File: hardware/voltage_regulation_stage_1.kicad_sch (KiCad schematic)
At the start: 21 parts, among them IC3 LT8333RDD#TRPBF

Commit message: Continued work on schematic.
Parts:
- added Q2: PMOS, symbol Simulation_SPICE:PMOS
- added Q5: MUN5314DW1T1G, Package_TO_SOT_SMD:SOT-363_SC-70-6, symbol Device:Q_Dual_NPN_PNP_BRT_E1B1C2E2B2C1
- added Q7: NMOS, symbol Simulation_SPICE:NMOS
- added R52, R53: R_Small_US, symbol Device:R_Small_US
- added R56, R57: ~, symbol Device:R_Small_US
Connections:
- net GND: now also Q7.1 (D), Q7.3 (S), R53.2, R57.2
- net VREG1_POWER: now reaches C34.1, L3.1
- net at C36.1, L4.2: now also Q2.3 (S), Q5.4 (E1), R56.1
- new net: Q2.2 (G), R56.2, R57.1
- new net: Q5.1 (E1), Q5.3 (C1), R52.1
- new net: Q5.5 (B1), Q5.6 (C1)
- new net: R52.2, R53.1
- new net VREG2_POWER: Q2.1 (D)
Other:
- moved on the sheet: C25, C26, C27, C28, C29, C30, C31, C32, C33, C34, C35, C36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

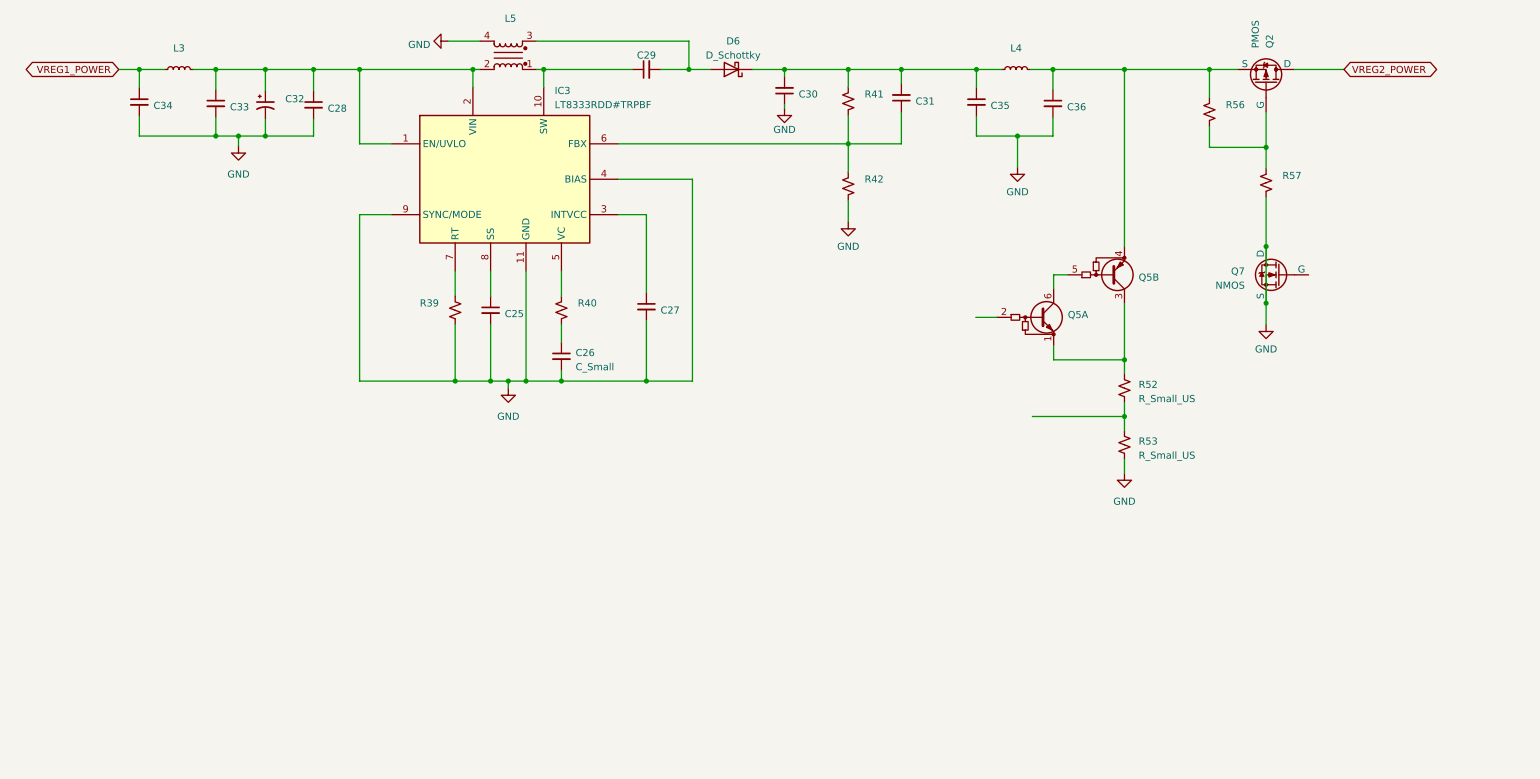
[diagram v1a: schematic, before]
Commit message: Component values chosen for bat. charge, bat. protect, USB input
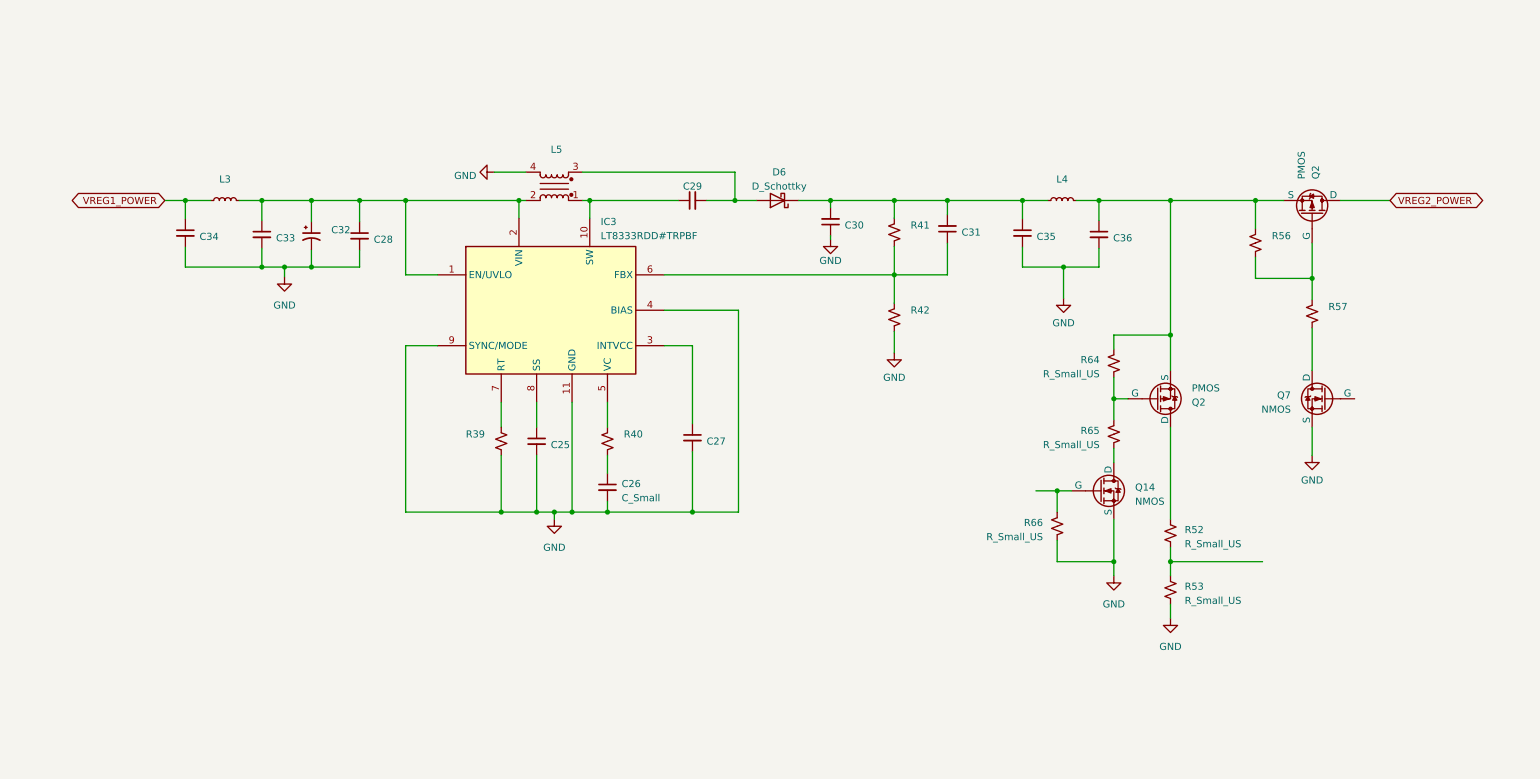
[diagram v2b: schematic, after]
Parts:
- removed Q5: MUN5314DW1T1G, Package_TO_SOT_SMD:SOT-363_SC-70-6, symbol Device:Q_Dual_NPN_PNP_BRT_E1B1C2E2B2C1
- added Q14: NMOS, symbol Simulation_SPICE:NMOS
- added Q2: PMOS, symbol Simulation_SPICE:PMOS
- added R64, R65, R66: R_Small_US, symbol Device:R_Small_US
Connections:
- net GND: now also Q14.3 (S), R66.2; no longer Q7.1 (D), R57.2
- net at C36.1, L4.2, Q2.3 (S)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: now also Q2.3 (S), R64.1
- net at R52.1: now also Q2.1 (D)
- new net: Q14.1 (D), R65.2
- new net: Q14.2 (G), R66.1
- new net: Q7.1 (D), R57.2
- new net: Q2.2 (G), R64.2, R65.1
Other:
- moved on the sheet: C25, C26, C27, C28, C29, C30, C31, C32, C33, C34, C35, C36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

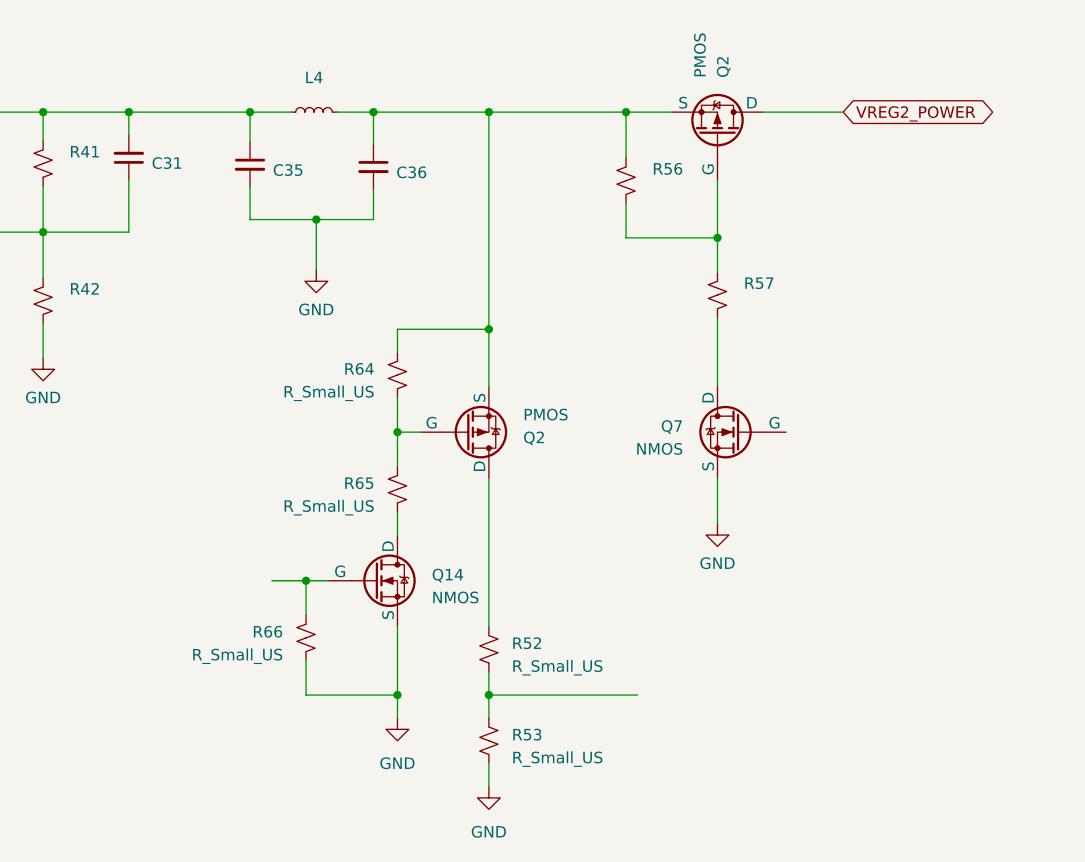
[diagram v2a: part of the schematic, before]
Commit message: Most work finished on stage1. Moving on to stage2.
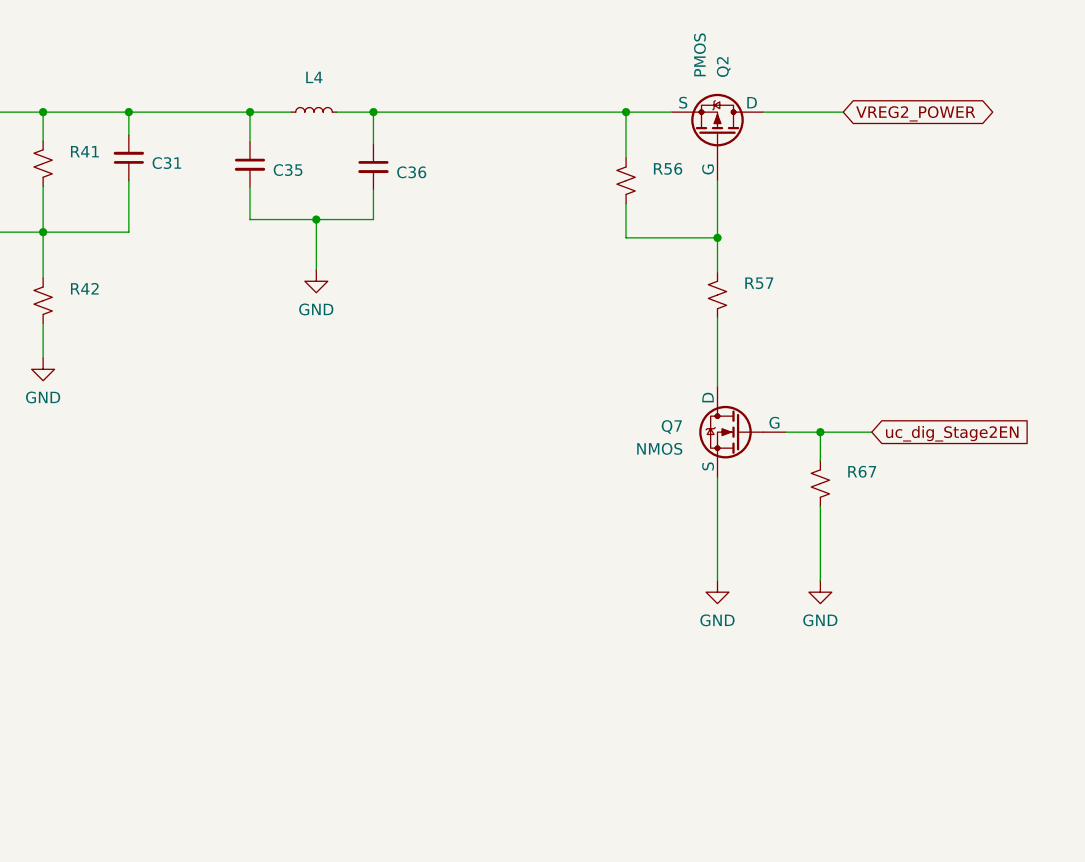
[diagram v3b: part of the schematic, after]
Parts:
- removed Q14: NMOS, symbol Simulation_SPICE:NMOS
- removed Q2: PMOS, symbol Simulation_SPICE:PMOS
- removed R52, R53, R64, R65, R66: R_Small_US, symbol Device:R_Small_US
- added R67: ~, symbol Device:R_Small_US
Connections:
- net GND: now also R67.2
- net uc_dig_Stage2EN: now reaches Q7.2 (G)
- net uc_dig_Stage2EN: now also R67.1

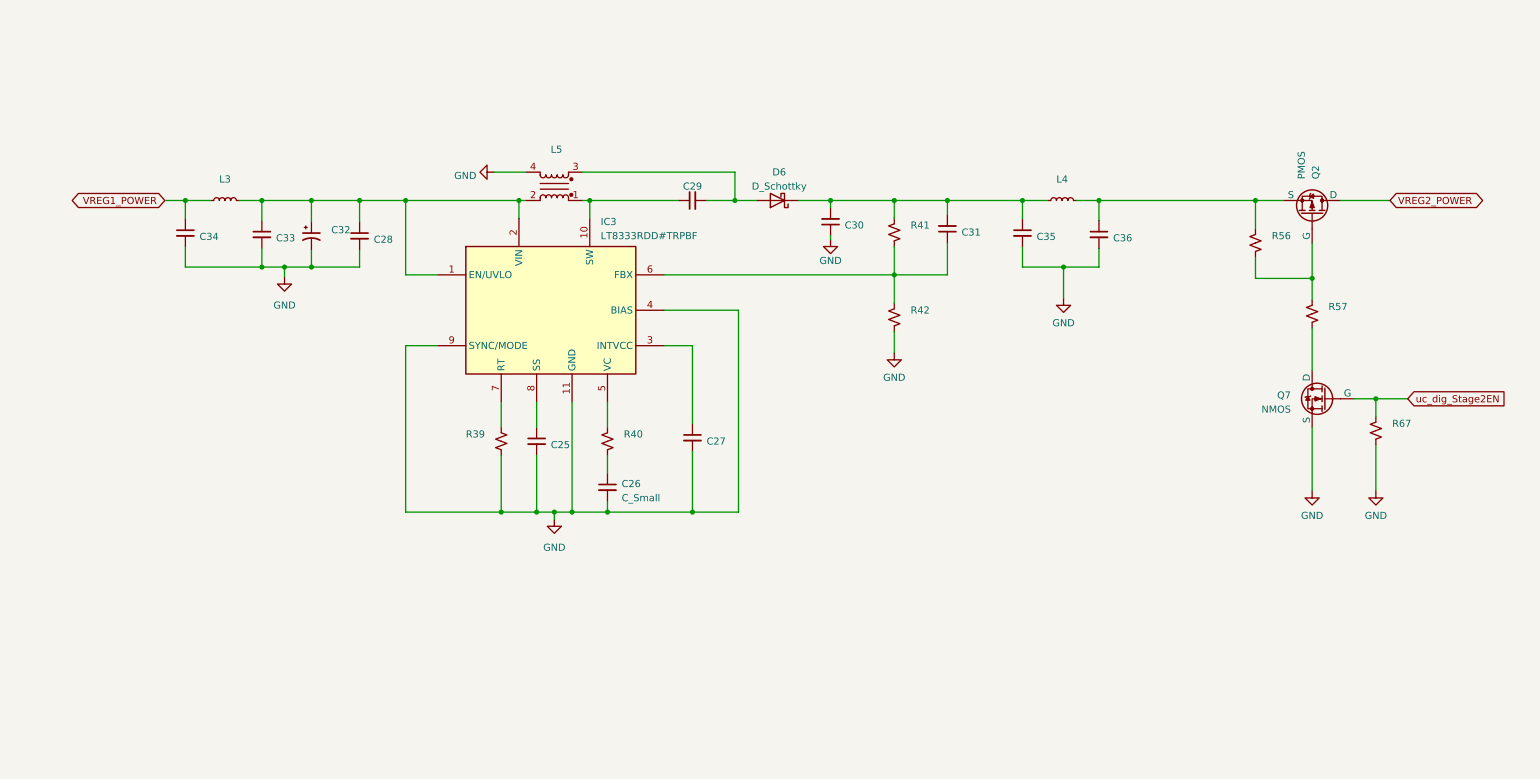
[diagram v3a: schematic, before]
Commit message: More simulation and work done on SEPIC stage. MOSFET changes to USB stage and charging stage.
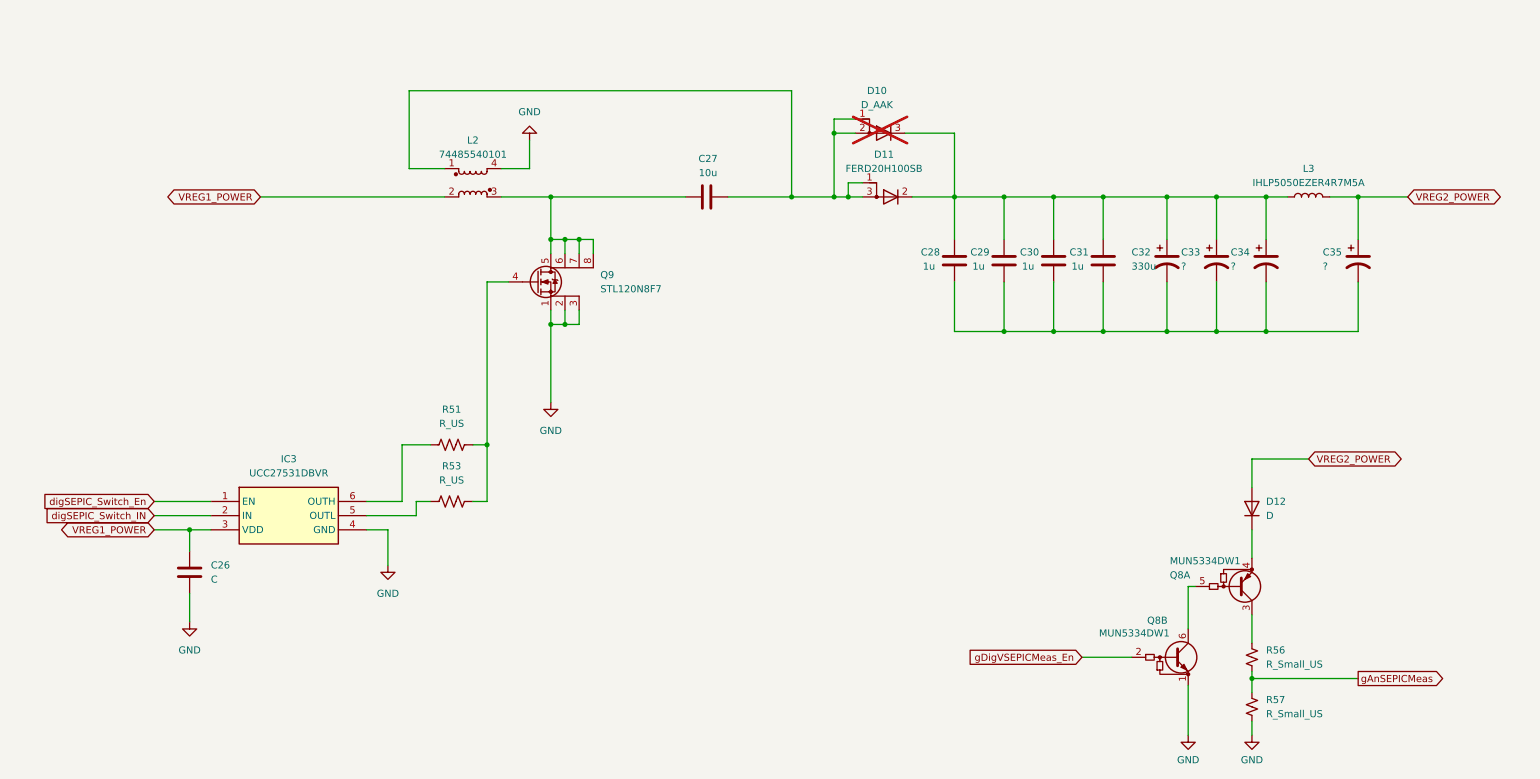
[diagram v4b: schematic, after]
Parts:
- removed C25, C27, C28, C29, C30, C31, C33, C34, C35, C36: ~, symbol Device:C_Small
- removed C26: C_Small, symbol Device:C_Small
- removed C32: C_Polarized_Small_US, symbol Device:C_Polarized_Small_US
- removed D6: D_Schottky, symbol Device:D_Schottky
- removed IC3: LT8333RDD#TRPBF, SON50P300X300X80-11N-D, symbol LT8333RDD#TRPBF:LT8333RDD#TRPBF
- removed L3, L4: L_Small, symbol Device:L_Small
- removed L5: L_Iron_Coupled, symbol Device:L_Iron_Coupled
- removed Q2: PMOS, symbol Simulation_SPICE:PMOS
- removed Q7: NMOS, symbol Simulation_SPICE:NMOS
- removed R39, R40, R41, R42, R67: ~, symbol Device:R_Small_US
- added C26: C, symbol Device:C
- added C27: 10u, symbol Device:C
- added C28, C29, C30, C31: 1u, symbol Device:C
- added C32: 330u, symbol Device:C_Polarized_US
- added C33, C34, C35: ?, symbol Device:C_Polarized_US
- added D10: D_AAK, Package_TO_SOT_SMD:TO-277A, symbol Device:D_AAK
- added D11: FERD20H100SB, symbol Daniel_Diode:D_AKA
- added D12: D, symbol Device:D
- added IC3: UCC27531DBVR, Package_TO_SOT_SMD:SOT-23-6, symbol Daniel_Gate-Driver:UCC27531DBVR
- added L2: 74485540101, Daniel_Inductor:74485540101, symbol Daniel_Inductor:L_Coupled
- added L3: IHLP5050EZER4R7M5A, Daniel_Inductor:IHLP-5050EZ, symbol Device:L
- added Q8: MUN5334DW1, Package_TO_SOT_SMD:SOT-363_SC-70-6, symbol Transistor_BJT:MUN5334DW1
- added Q9: STL120N8F7, Package_SON:ST_PowerFLAT-6L_5x6mm_P1.27mm, symbol Daniel_NMOS:Q_NMOS_DGS
- added R51, R53: R_US, symbol Device:R_US
- R56, R57: value ~ -> R_Small_US
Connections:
- net GND: now also R57.1, C26.2, IC3.4 (GND), L2.4, Q8.1 (E2), Q9.1 (S), Q9.2 (S), Q9.3 (S)
- net VREG1_POWER: now also C26.1, IC3.3 (VDD), L2.2
- net VREG2_POWER: now also C35.1, D12.2 (A), L3.2
- net gAnSEPICMeas: now reaches R56.1
- net gAnSEPICMeas: now also R57.2
- net at R56.2: now also Q8.3 (C1); no longer R57.1
- new net: IC3.5 (OUTL), R53.1
- new net: Q9.4 (G), R51.2, R53.2
- new net: C27.2, D10.1 (A), D10.2 (A), D11.1 (A), D11.3 (A), L2.1
- new net: C28.2, C29.2, C30.2, C31.2, C32.1, C33.1, C34.1, D10.3 (K), D11.2 (K), L3.1
- new net: C28.1, C29.1, C30.1, C31.1, C32.2, C33.2, C34.2, C35.2
- new net: D12.1 (K), Q8.4 (E1)
- new net: Q8.5 (B1), Q8.6 (C2)
- new net: IC3.6 (OUTH), R51.1
- new net: C27.1, L2.3, Q9.5 (D), Q9.6 (D), Q9.7 (D), Q9.8 (D)
- new net digSEPIC_Switch_En: IC3.1 (EN)
- new net digSEPIC_Switch_IN: IC3.2 (IN)
- new net gDigVSEPICMeas_En: Q8.2 (B2)
